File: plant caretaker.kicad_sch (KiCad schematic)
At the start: 2 parts, among them J1 694106402002

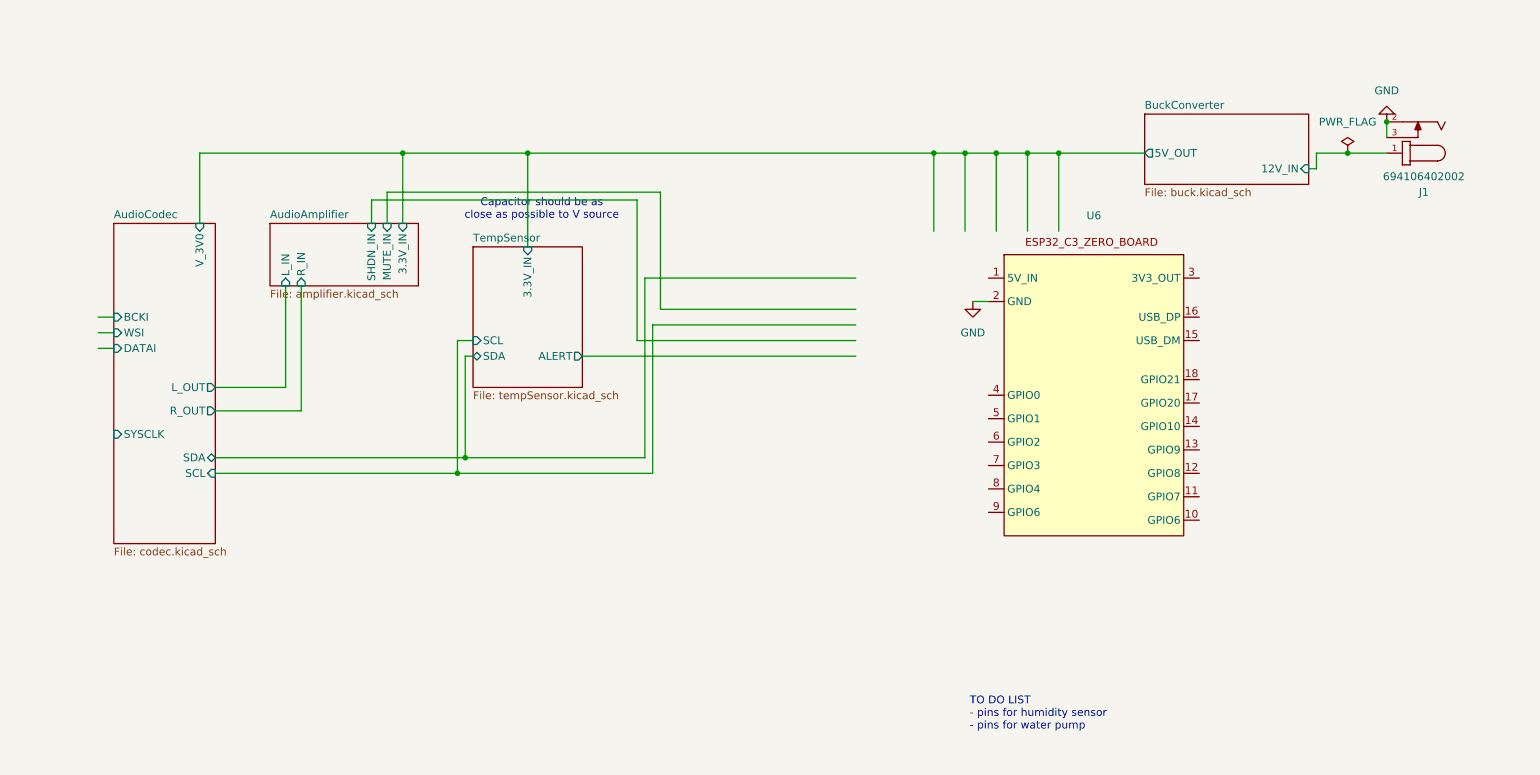
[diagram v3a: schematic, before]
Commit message: Connected ESP32 and other components
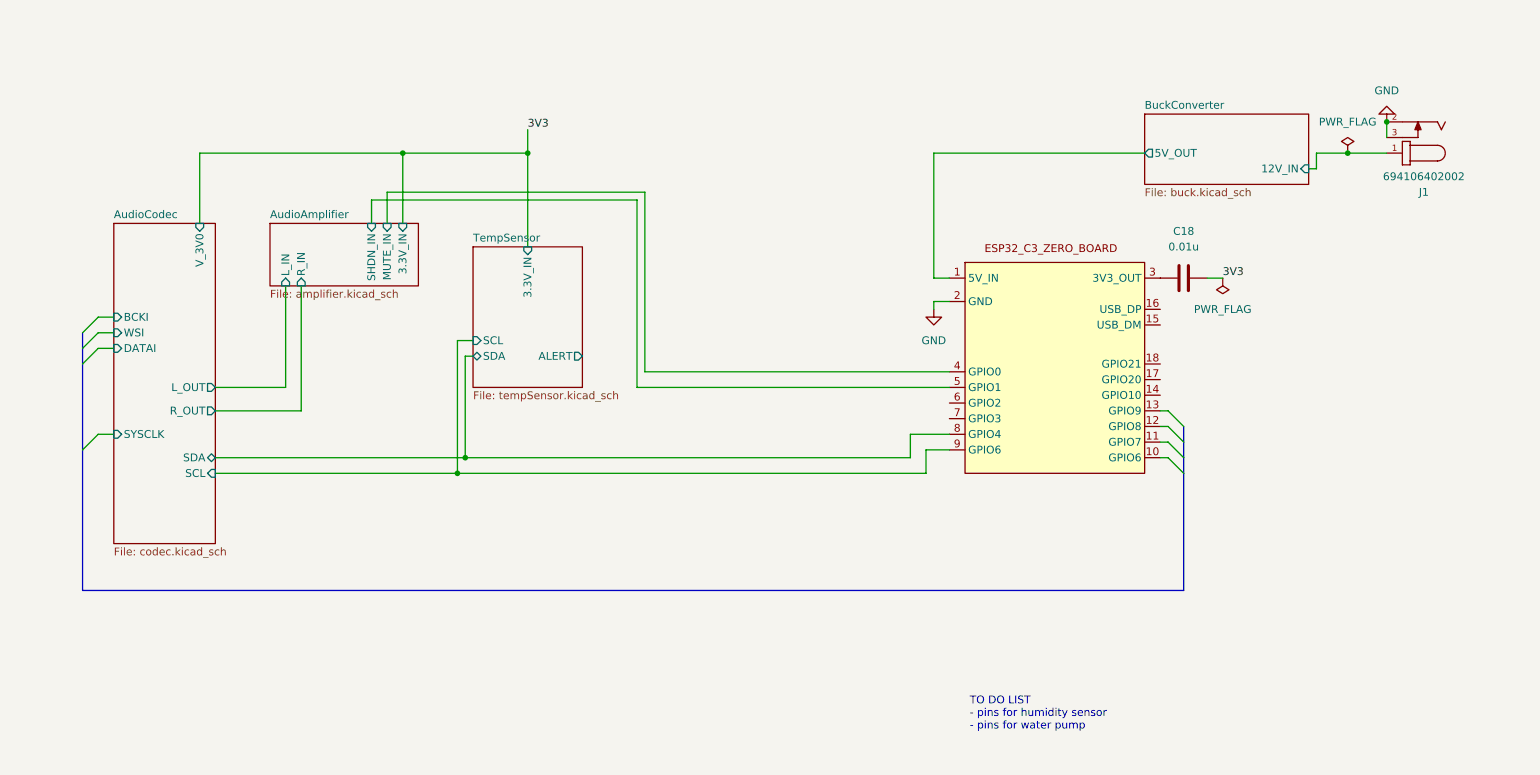
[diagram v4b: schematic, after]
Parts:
- added C18: 0.01u, symbol Device:C
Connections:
- net AudioAmplifier/MUTE_IN: now also U6.4 (GPIO0)
- net AudioAmplifier/SHDN_IN: now also U6.5 (GPIO1)
- net AudioCodec/SCL: now also U6.9 (GPIO6)
- net AudioCodec/SDA: now also U6.8 (GPIO4)
- net BuckConverter/5V_OUT: now reaches U6.1 (5V_IN)
- net at U6.3 (3V3_OUT): now also C18.1
- new net 3V3: C18.2
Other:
- note removed: "Capacitor should be as close as possible to V source"

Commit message: Finished connecting ICs to ESP32
Also fixed bus connection
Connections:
- net TempSensor/ALERT: now also U6.6 (GPIO2)
- net CODEC.SYSCLK: now reaches U6.10 (GPIO6)
- net CODEC.DATAI: now reaches U6.11 (GPIO7)
- net CODEC.WSI: now reaches U6.12 (GPIO8)
- net CODEC.BCKI: now reaches U6.13 (GPIO9)

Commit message: Added Lil Pump
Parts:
- added D2: D, symbol Device:D
- added J2: Conn_01x02_Pin, symbol Connector:Conn_01x02_Pin
- added Q1: IRFZ44N, IRFZ44N:TO254P1016X419X2286-3, symbol IRFZ44N:IRFZ44N
- added R10: 1k, symbol Device:R
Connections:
- net BuckConverter/12V_IN: now also D2.1 (K), J2.2 (Pin_2)
- net GND: now also Q1.3
- net at U6.18 (GPIO21): now also R10.1
- new net: D2.2 (A), J2.1 (Pin_1), Q1.2
- new net: Q1.1, R10.2
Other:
- note added: "GND of the pump"
- note added: "V+ of the pump"

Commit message: Swapped MOSFET
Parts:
- removed Q1: IRFZ44N, IRFZ44N:TO254P1016X419X2286-3, symbol IRFZ44N:IRFZ44N
- added Q3: FDMS86255, Package_TO_SOT_SMD:TDSON-8-1, symbol Transistor_FET:FDMS86255
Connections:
- net GND: now also Q3.1 (S), Q3.2 (S), Q3.3 (S)
- net at D2.2 (A), J2.1 (Pin_1): now also Q3.5 (D)
- net at R10.2: now also Q3.4 (G)
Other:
- moved on the sheet: R10
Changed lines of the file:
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@@
 	(wire
 		(pts
-			(xy 241.3 71.12) (xy 241.3 88.9)
-		)
-		(stroke
-			(width 0)
-			(type default)
-		)
-	)
-	(wire
-		(pts
-			(xy 248.92 72.39) (xy 248.92 71.12)
+			(xy 241.3 69.85) (xy 241.3 88.9)
 		)
 		(stroke
@@
 		(pts
 			(xy 39.37 88.9) (xy 39.37 102.87)
-		)
-		(stroke
-			(width 0)
-			(type default)
-		)
-	)
-	(wire
-		(pts
-			(xy 251.46 72.39) (xy 248.92 72.39)
 		)
 		(stroke
@@
 	)
 	(symbol
+		(lib_id "Transistor_FET:FDMS86255")
+		(at 254 69.85 0)
+		(unit 1)
+		(exclude_from_sim no)
+		(in_bom yes)
+		(on_board yes)
+		(dnp no)
+		(fields_autoplaced yes)
+		(property "Reference" "Q3"
+			(at 260.35 68.5799 0)
+			(effects
+				(font
+					(size 1.27 1.27)
+				)
+				(justify left)
+			)
+		)
+		(property "Value" "FDMS86255"
+			(at 260.35 71.1199 0)
+			(effects
+				(font
+					(size 1.27 1.27)
+				)
+				(justify left)
+			)
+		)
+		(property "Footprint" "Package_TO_SOT_SMD:TDSON-8-1"
+			(at 259.08 71.755 0)
+			(effects
+				(font
+					(size 1.27 1.27)
+					(italic yes)
+				)
+				(justify left)
+				(hide yes)
+			)
+		)
+		(property "Datasheet" "https://www.onsemi.com/pub/Collateral/FDMS86255-D.pdf"
+			(at 259.08 73.66 0)
+			(effects
+				(font
+					(size 1.27 1.27)
+				)
+				(justify left)
+				(hide yes)
+			)
+		)
+		(property "Description" "10A Id, 150V Vds, N-Channel Shielded Gate PowerTrench MOSFET, 12.4mOhm Ron, 63nC Qgmax, -55 to 150 °C, 5x6mm SON8"
+			(at 254 69.85 0)
+			(effects
+				(font
+					(size 1.27 1.27)
+				)
+				(hide yes)
+			)
+		)
+		(pin "2"
+		)
+		(pin "3"
+		)
+		(pin "5"
+		)
+		(pin "1"
+		)
+		(pin "4"
+		)
+		(instances
+			(project ""
+				(path "/23b35dcc-615e-4aec-abee-c26cc3d8b906"
+					(reference "Q3")
+					(unit 1)
+				)
+			)
+		)
+	)
+	(symbol
 		(lib_id "power:GND")
 		(at 262.89 49.53 180)
@@
 	(symbol
 		(lib_id "Device:R")
-		(at 245.11 71.12 90)
+		(at 245.11 69.85 90)
 		(unit 1)
 		(exclude_from_sim no)
@@
 		(fields_autoplaced yes)
 		(property "Reference" "R10"
-			(at 245.11 64.77 90)
+			(at 245.11 63.5 90)
 			(effects
 				(font
@@
 		)
 		(property "Value" "1k"
-			(at 245.11 67.31 90)
+			(at 245.11 66.04 90)
 			(effects
 				(font
@@
 		)
 		(property "Footprint" ""
-			(at 245.11 72.898 90)
+			(at 245.11 71.628 90)
 			(effects
 				(font
@@
 		)
 		(property "Datasheet" "~"
-			(at 245.11 71.12 0)
+			(at 245.11 69.85 0)
 			(effects
 				(font
@@
 		)
 		(property "Description" "Resistor"
-			(at 245.11 71.12 0)
+			(at 245.11 69.85 0)
 			(effects
 				(font
@@
 					(unit 1)
 				)
-			)
-		)
-	)
-	(symbol
-		(lib_id "IRFZ44N:IRFZ44N")
-		(at 254 69.85 0)
-		(unit 1)
-		(exclude_from_sim no)
-		(in_bom yes)
-		(on_board yes)
-		(dnp no)
-		(fields_autoplaced yes)
-		(property "Reference" "Q1"
-			(at 260.35 68.5799 0)
-			(effects
-				(font
-					(size 1.27 1.27)
-				)
-				(justify left)
-			)
-		)
-		(property "Value" "IRFZ44N"
-			(at 260.35 71.1199 0)
-			(effects
-				(font
-					(size 1.27 1.27)
-				)
-				(justify left)
-			)
-		)
-		(property "Footprint" "IRFZ44N:TO254P1016X419X2286-3"
-			(at 254 69.85 0)
-			(effects
-				(font
-					(size 1.27 1.27)
-				)
-				(justify bottom)
-				(hide yes)
-			)
-		)
-		(property "Datasheet" ""
-			(at 254 69.85 0)
-			(effects
-				(font
-					(size 1.27 1.27)
-				)
-				(hide yes)
-			)
-		)
-		(property "Description" ""
-			(at 254 69.85 0)
-			(effects
-				(font
-					(size 1.27 1.27)
-				)
-				(hide yes)
-			)
-		)
-		(property "MF" "Infineon Technologies"
-			(at 254 69.85 0)
-			(effects
-				(font
-					(size 1.27 1.27)
-				)
-				(justify bottom)
-				(hide yes)
-			)
-		)
-		(property "MAXIMUM_PACKAGE_HEIGHT" "22.86 mm"
-			(at 254 69.85 0)
-			(effects
-				(font
-					(size 1.27 1.27)
-				)
-				(justify bottom)
-				(hide yes)
-			)
-		)
-		(property "Package" "TO-220-3 Infineon"
-			(at 254 69.85 0)
-			(effects
-				(font
-					(size 1.27 1.27)
-				)
-				(justify bottom)
-				(hide yes)
-			)
-		)
-		(property "Price" "None"
-			(at 254 69.85 0)
-			(effects
-				(font
-					(size 1.27 1.27)
-				)
-				(justify bottom)
-				(hide yes)
-			)
-		)
-		(property "Check_prices" "https://www.snapeda.com/parts/IRFZ44N/Infineon/view-part/?ref=eda"
-			(at 254 69.85 0)
-			(effects
-				(font
-					(size 1.27 1.27)
-				)
-				(justify bottom)
-				(hide yes)
-			)
-		)
-		(property "STANDARD" "IPC 7351B"
-			(at 254 69.85 0)
-			(effects
-				(font
-					(size 1.27 1.27)
-				)
-				(justify bottom)
-				(hide yes)
-			)
-		)
-		(property "PARTREV" "09/21/10"
-			(at 254 69.85 0)
-			(effects
-				(font
-					(size 1.27 1.27)
-				)
-				(justify bottom)
-				(hide yes)
-			)
-		)
-		(property "SnapEDA_Link" "https://www.snapeda.com/parts/IRFZ44N/Infineon/view-part/?ref=snap"
-			(at 254 69.85 0)
-			(effects
-				(font
-					(size 1.27 1.27)
-				)
-				(justify bottom)
-				(hide yes)
-			)
-		)
-		(property "MP" "IRFZ44N"
-			(at 254 69.85 0)
-			(effects
-				(font
-					(size 1.27 1.27)
-				)
-				(justify bottom)
-				(hide yes)
-			)
-		)
-		(property "Description_1" "\n                        \n                            N-Channel 55 V 49A (Tc) 94W (Tc) Through Hole TO-220AB\n                        \n"
-			(at 254 69.85 0)
-			(effects
-				(font
-					(size 1.27 1.27)
-				)
-				(justify bottom)
-				(hide yes)
-			)
-		)
-		(property "SNAPEDA_PN" "IRFZ44N"
-			(at 254 69.85 0)
-			(effects
-				(font
-					(size 1.27 1.27)
-				)
-				(justify bottom)
-				(hide yes)
-			)
-		)
-		(property "Availability" "In Stock"
-			(at 254 69.85 0)
-			(effects
-				(font
-					(size 1.27 1.27)
-				)
-				(justify bottom)
-				(hide yes)
-			)
-		)
-		(property "MANUFACTURER" "Infineon"
-			(at 254 69.85 0)
-			(effects
-				(font
-					(size 1.27 1.27)
-				)
-				(justify bottom)
-				(hide yes)
-			)
-		)
-		(pin "2"
-		)
-		(pin "1"
-		)
-		(pin "3"
-		)
-		(instances
-			(project ""
-				(path "/23b35dcc-615e-4aec-abee-c26cc3d8b906"
-					(reference "Q1")
-					(unit 1)
-				)

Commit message: Added Kitronik and cleaned connections
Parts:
- added J3: Kitronik, symbol Connector:Conn_01x03_Socket
- J2: value Conn_01x02_Pin -> Water_Pump
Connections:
- net GND: now also J3.1 (Pin_1)
- net at U6.7 (GPIO3): now also J3.2 (Pin_2)
- net 3V3 renamed +3V3
- net +3V3: now also J3.3 (Pin_3)
- no-connect marks 0 -> 4
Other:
- note removed: "GND of the pump"
- note removed: "V+ of the pump"
- moved on the sheet: D2, J1, J2, Q3, R10
